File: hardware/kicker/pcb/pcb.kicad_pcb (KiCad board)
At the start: 2 copper layers, 108.7 x 42.8 mm, 35 parts, among them J1 Conn_01x04, J2 Conn_01x04, J3 Conn_01x02, Q1 NMOS, U1 XL6019E1, U2 TS4535TP 250GF 009, U4 TC4427AEOA713_C5804606

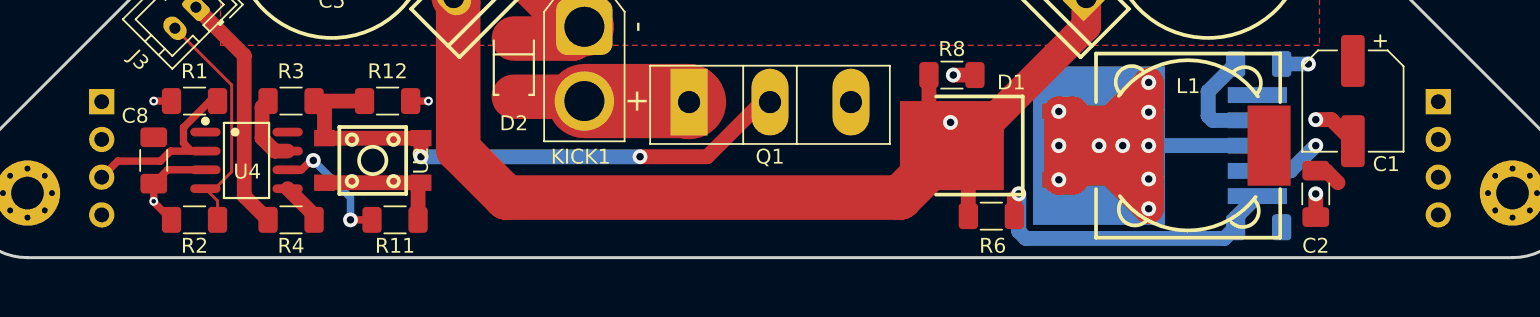
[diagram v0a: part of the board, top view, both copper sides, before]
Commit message: fixed non convention following of kicker pcb
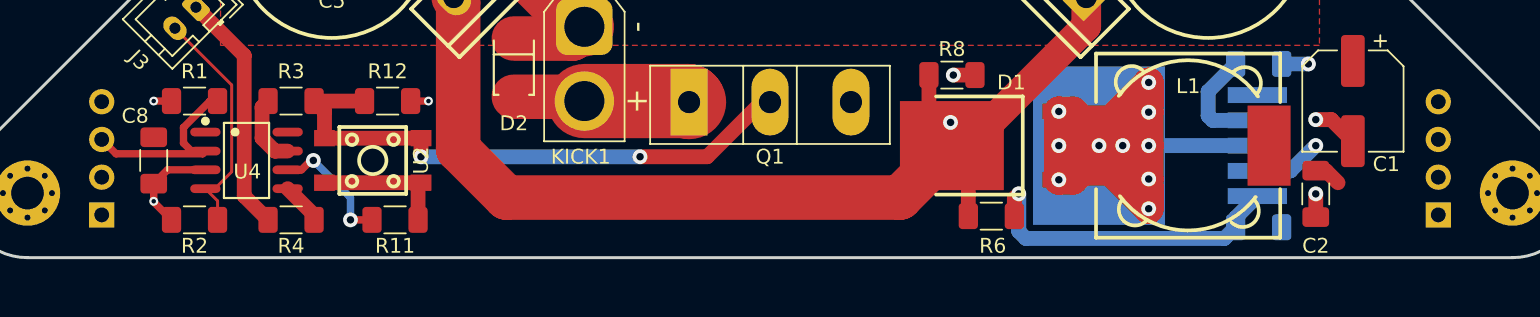
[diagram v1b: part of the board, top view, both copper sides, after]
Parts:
- moved J1 7.62 mm to (45.0, -2.88), turned to 0 degrees
- moved J2 7.62 mm to (-45.0, -2.88), turned to 0 degrees
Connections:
- J1 pad 1: VCC -> GND
- J1 pad 2: VCC -> GND
- J1 pad 3: GND -> VCC
- J1 pad 4: GND -> VCC
